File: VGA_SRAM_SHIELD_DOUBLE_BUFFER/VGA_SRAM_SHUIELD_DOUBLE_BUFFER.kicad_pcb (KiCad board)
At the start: 6 copper layers, 125 x 53.5 mm, 53 parts, among them J1 USB_A_Stacked, J2 ANALOG, J3 Mini-DIN-6, J4 PWR AUX, J5 ISP, J6 Micro_SD_Card, J7 DE15_Receptacle_HighDensity, J8 AUDIO, U1 74HC245, U10 74HC245, U11 74HC245, U12 74LS08, U13 74LS32, U14 DATA_BANK1, U15 DATA_BANK2, U16 74HC245, U17 74HC245, U18 74HC245, U19 K6X8008T2B-TF55, U2 74HC245, U20 K6X8008T2B-TF55, U21 74HC245, U22 74HC245, U3 74HC245, U5 74HC245, U6 74HC245, U7 74HC245, U8 74HC14, U9 74HC245, X1 TCXO-14

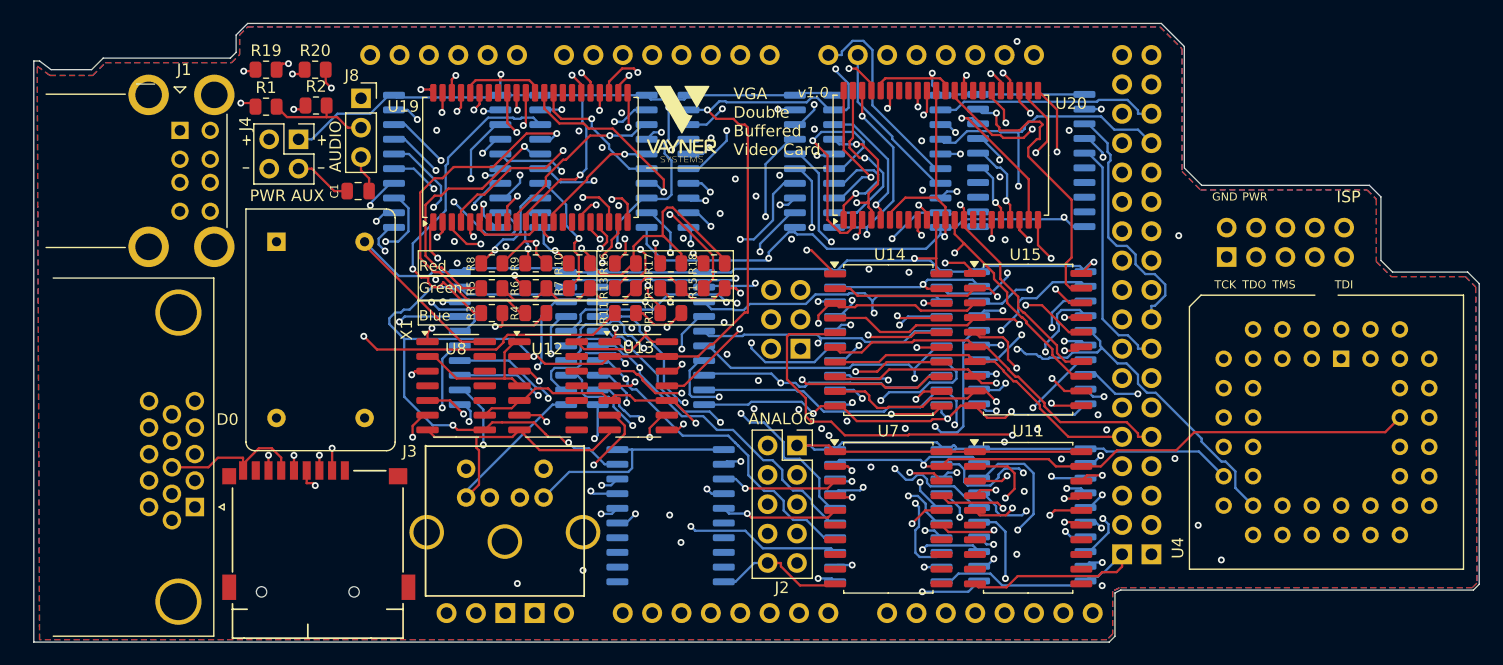
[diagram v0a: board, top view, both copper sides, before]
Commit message: remove second vga resistor network
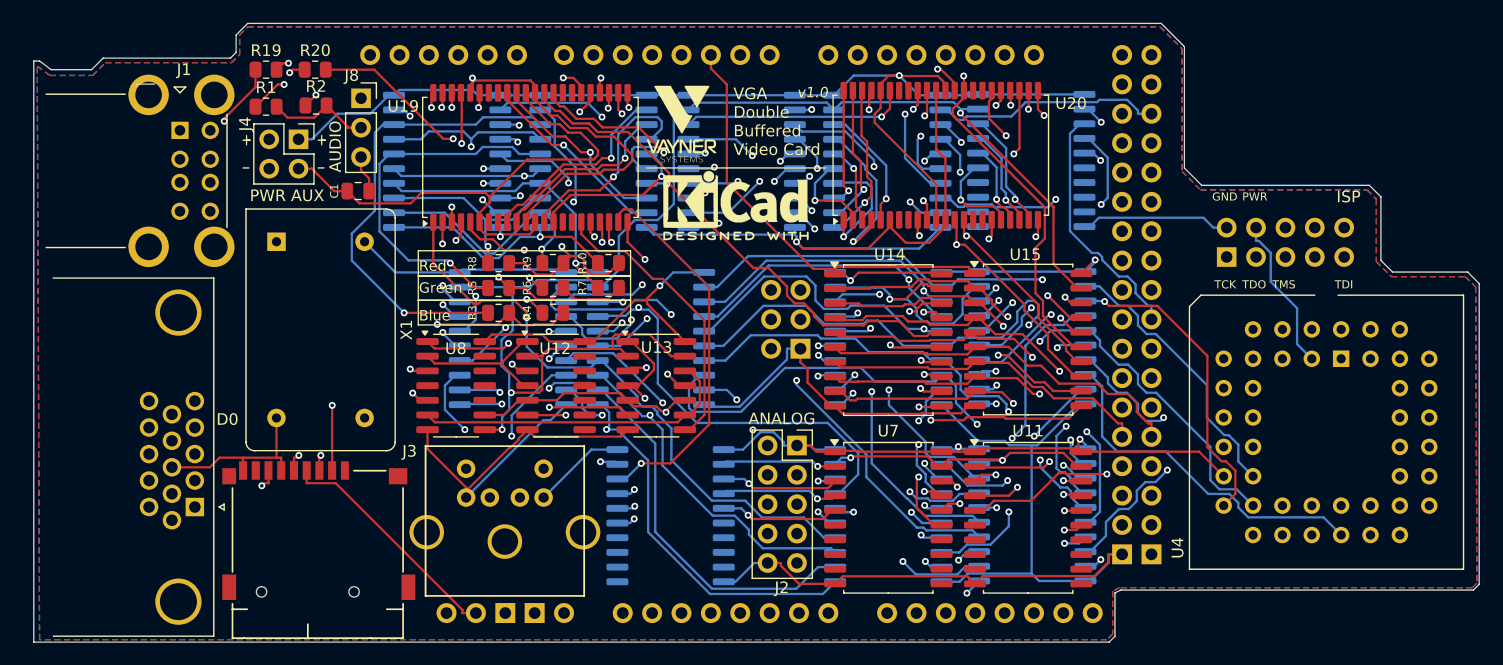
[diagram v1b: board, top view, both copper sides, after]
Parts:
- removed R11: R800, Resistor_SMD:R_0805_2012Metric
- removed R12, R15, R18: R470, Resistor_SMD:R_0805_2012Metric
- removed R13, R17: R1.8K, Resistor_SMD:R_0805_2012Metric
- removed R14: R1.2K, Resistor_SMD:R_0805_2012Metric
- removed R16: R2.2K, Resistor_SMD:R_0805_2012Metric
- added REF**: KiCad-Logo2_5mm_SilkScreen, Symbol:KiCad-Logo2_5mm_SilkScreen, F.Cu at (88.2, 146.7)
- J7: value DE15_Receptacle_HighDensity -> VGA D-SUB15
- U4: value ~ -> ATF1504AS
- moved R10 2.51 mm to (77.2, 151.7)
- moved R7 2.51 mm to (77.2, 153.9)
- moved U13 1.56 mm to (81.3, 162.3)
- moved R4 1.49 mm to (72.4, 156.0)
- moved R6 1.49 mm to (72.4, 153.9)
- moved R9 1.49 mm to (72.4, 151.7)
- moved U12 0.69 mm to (72.7, 162.3)
- moved R3 0.59 mm to (67.7, 156.0)
- moved R5 0.59 mm to (67.7, 153.9)
- moved R8 0.59 mm to (67.7, 151.7)
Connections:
- net Net-(J7-Pad1) renamed RED
- net Net-(J7-Pad2) renamed GREEN
- net Net-(J7-Pad3) renamed BLUE
- U22 pad 11: Net-(U22-B7) -> Net-(U21-B7)
- U22 pad 12: Net-(U22-B6) -> Net-(U21-B6)
- U22 pad 13: Net-(U22-B5) -> Net-(U21-B5)
- U22 pad 14: Net-(U22-B4) -> Net-(U21-B4)
- U22 pad 15: Net-(U22-B3) -> Net-(U21-B3)
- U22 pad 16: Net-(U22-B2) -> Net-(U21-B2)
- U22 pad 17: Net-(U22-B1) -> Net-(U21-B1)
- U22 pad 18: Net-(U22-B0) -> Net-(U21-B0)
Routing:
- net ~{VGA_OUT}: track 133.3 -> 78.6 mm, vias 2 -> 1
- net Net-(U22-B0): track 47.3 -> 0.00 mm, vias 2 -> 0
- net MEMADDR_BANK19: track 128.2 -> 84.6 mm, vias 4 -> 3
- net Net-(U21-B3): track 66.7 -> 23.8 mm, vias 3 -> 2
- net COUNTER_MEMADDR14: track 84.1 -> 125.9 mm, vias 2 -> 1
- net ~{COUNTER_BANK1}: track 167.3 -> 128.0 mm, vias 6 -> 4
- net Net-(U22-B4): track 38.7 -> 0.00 mm, vias 2 -> 0
- net GREEN: track 80.0 -> 46.1 mm
- net Net-(U22-B3): track 33.4 -> 0.00 mm, vias 3 -> 0
- net Net-(U22-B1): track 32.9 -> 0.00 mm, vias 3 -> 0
- net Net-(U22-B2): track 32.3 -> 0.00 mm, vias 2 -> 0
- net MEMADDR_BANK26: track 63.8 -> 31.5 mm
- net Net-(U22-B7): track 31.6 -> 0.00 mm, vias 2 -> 0
- net MEMADDR_BANK23: track 53.9 -> 22.4 mm, vias 3 -> 2
- net Net-(U22-B5): track 30.0 -> 0.00 mm, vias 2 -> 0
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
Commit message: updates to double buffer and multiplexed, 2xatf1508 concept
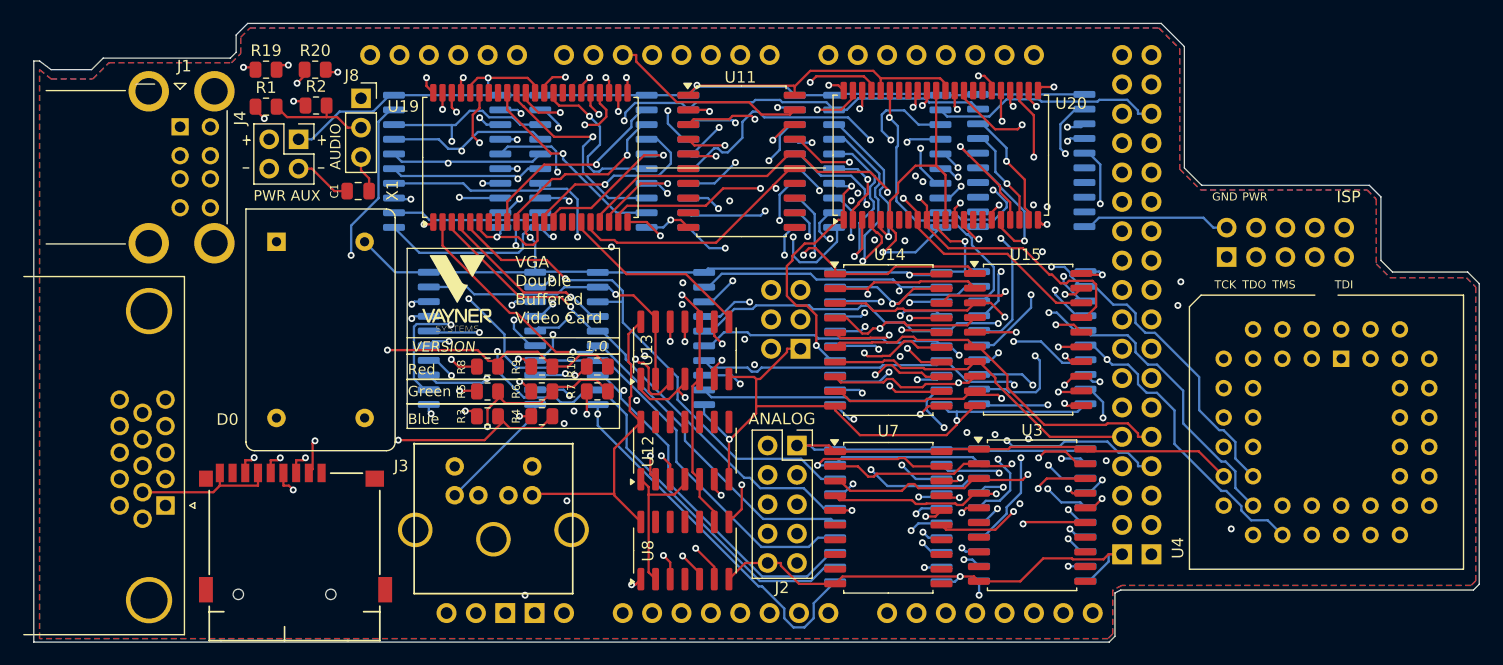
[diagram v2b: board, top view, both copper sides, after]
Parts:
- removed REF**: KiCad-Logo2_5mm_SilkScreen, Symbol:KiCad-Logo2_5mm_SilkScreen
- U3: moved to F.Cu
- moved U11 39.6 mm to (88.7, 142.9)
- moved U3 31.3 mm to (113.8, 173.5), turned to 0 degrees
- moved U8 24.4 mm to (83.8, 176.6), turned to 90 degrees
- moved U12 12.5 mm to (83.8, 167.9), turned to 90 degrees
- moved R5 9.00 mm to (66.7, 162.8)
- moved R8 9.00 mm to (66.7, 160.7)
- moved R10 9.00 mm to (76.2, 160.7)
- moved R3 9.00 mm to (66.7, 165.0)
- moved R7 9.00 mm to (76.2, 162.8)
- moved R4 9.00 mm to (71.4, 165.0)
- moved R6 9.00 mm to (71.4, 162.8)
- moved R9 9.00 mm to (71.4, 160.7)
- moved U13 3.92 mm to (83.8, 159.3), turned to 90 degrees
- moved U2 2.68 mm to (66.3, 158.2)
- moved J7 2.54 mm to (38.9, 172.7)
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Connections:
- A1 pad D5: unconnected-(A1-PadD5) -> BANK_SELECT
- U19 pad 10: DATA_BANK16 -> DATA_BANK11
- U19 pad 13: DATA_BANK15 -> DATA_BANK12
- U19 pad 14: DATA_BANK14 -> DATA_BANK13
- U19 pad 31: DATA_BANK13 -> DATA_BANK14
- U19 pad 32: DATA_BANK12 -> DATA_BANK15
- U19 pad 35: DATA_BANK11 -> DATA_BANK16
- U19 pad 36: DATA_BANK10 -> DATA_BANK17
- U19 pad 9: DATA_BANK17 -> DATA_BANK10
- U20 pad 10: DATA_BANK26 -> DATA_BANK21
- U20 pad 13: DATA_BANK25 -> DATA_BANK22
- U20 pad 14: DATA_BANK24 -> DATA_BANK23
- U20 pad 31: DATA_BANK23 -> DATA_BANK24
- U20 pad 32: DATA_BANK22 -> DATA_BANK25
- U20 pad 35: DATA_BANK21 -> DATA_BANK26
- U20 pad 36: DATA_BANK20 -> DATA_BANK27
- U20 pad 9: DATA_BANK27 -> DATA_BANK20
- U21 pad 2: DATA_BANK17 -> DATA_BANK10
- U21 pad 3: DATA_BANK16 -> DATA_BANK11
- U21 pad 4: DATA_BANK15 -> DATA_BANK12
- U21 pad 5: DATA_BANK14 -> DATA_BANK13
- U21 pad 6: DATA_BANK13 -> DATA_BANK14
- U21 pad 7: DATA_BANK12 -> DATA_BANK15
- U21 pad 8: DATA_BANK11 -> DATA_BANK16
- U21 pad 9: DATA_BANK10 -> DATA_BANK17
- U22 pad 2: DATA_BANK27 -> DATA_BANK20
- U22 pad 3: DATA_BANK26 -> DATA_BANK21
- U22 pad 4: DATA_BANK25 -> DATA_BANK22
- U22 pad 5: DATA_BANK24 -> DATA_BANK23
- U22 pad 6: DATA_BANK23 -> DATA_BANK24
- U22 pad 7: DATA_BANK22 -> DATA_BANK25
- U22 pad 8: DATA_BANK21 -> DATA_BANK26
- U22 pad 9: DATA_BANK20 -> DATA_BANK27
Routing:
- net BANK_SELECT: track 136.1 -> 215.0 mm, vias 4 -> 3
- net COUNTER_MEMADDR14: track 125.9 -> 82.7 mm, vias 1 -> 2
- net COUNTER_MEMADDR8: track 111.1 -> 74.0 mm, vias 1 -> 2
- net GND: track 509.4 -> 481.7 mm, vias 2 -> 8
- net MCUMEMADDR7: track 83.8 -> 111.2 mm
- net ~{COUNTER_BANK1}: track 128.0 -> 154.9 mm, vias 4 -> 6
- net PWR: track 437.2 -> 411.6 mm, vias 7 -> 6
- net MEMADDR_BANK115: track 68.2 -> 91.9 mm, vias 3 -> 4
- net ~{OE_BANK1}: track 26.9 -> 48.3 mm
- net COUNTER_MEMADDR17: track 69.5 -> 48.9 mm
- net DATA_BANK22: track 81.5 -> 61.1 mm
- net COUNTER_MEMADDR19: track 74.5 -> 54.5 mm, vias 1 -> 2
- net COUNTER_MEMADDR13: track 78.7 -> 97.9 mm, vias 2 -> 3
- net Net-(U21-B5): track 18.1 -> 36.4 mm, vias 1 -> 3
- net DATA0: track 39.3 -> 57.3 mm, vias 1 -> 2
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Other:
- board text added: "1.0"
- board text added: "VERSION"
- board text removed: "v1.0"
